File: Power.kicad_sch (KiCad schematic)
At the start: 45 parts, among them J6 Screw_Terminal_01x03, T1 230/6, T2 78250MC-R, U3 LF50_TO252, U4 LD3985G33R_TSOT23, U5 SN6507DGQ, U6 LD3985G33R_TSOT23

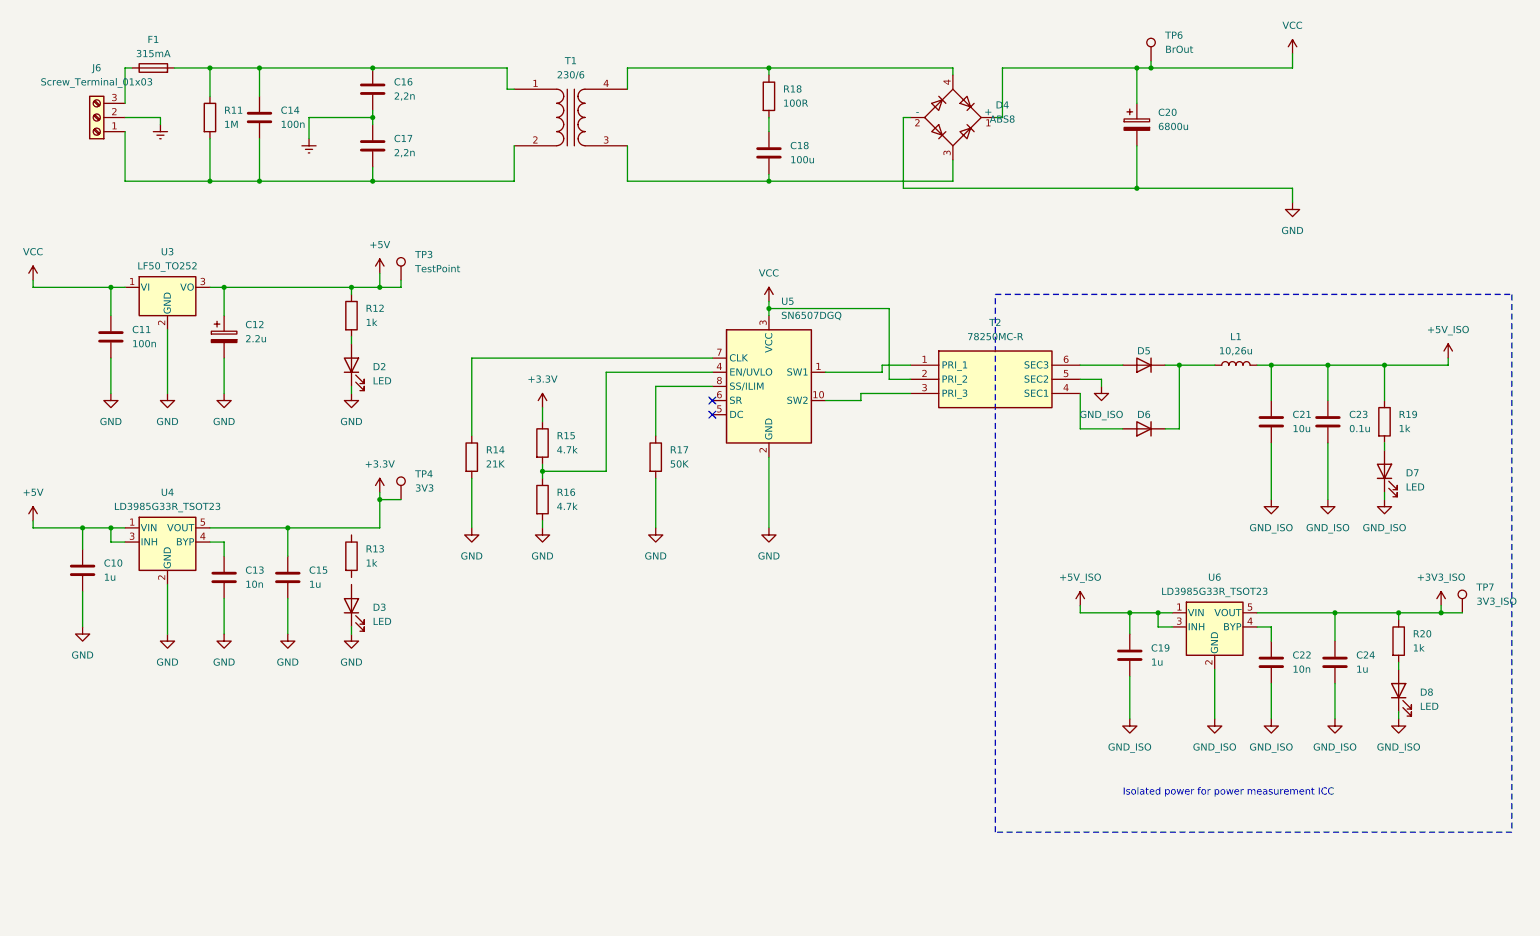
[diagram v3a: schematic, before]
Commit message: Footprints and elements update
Added another batch of footprints and links to the elements. More coming soon.
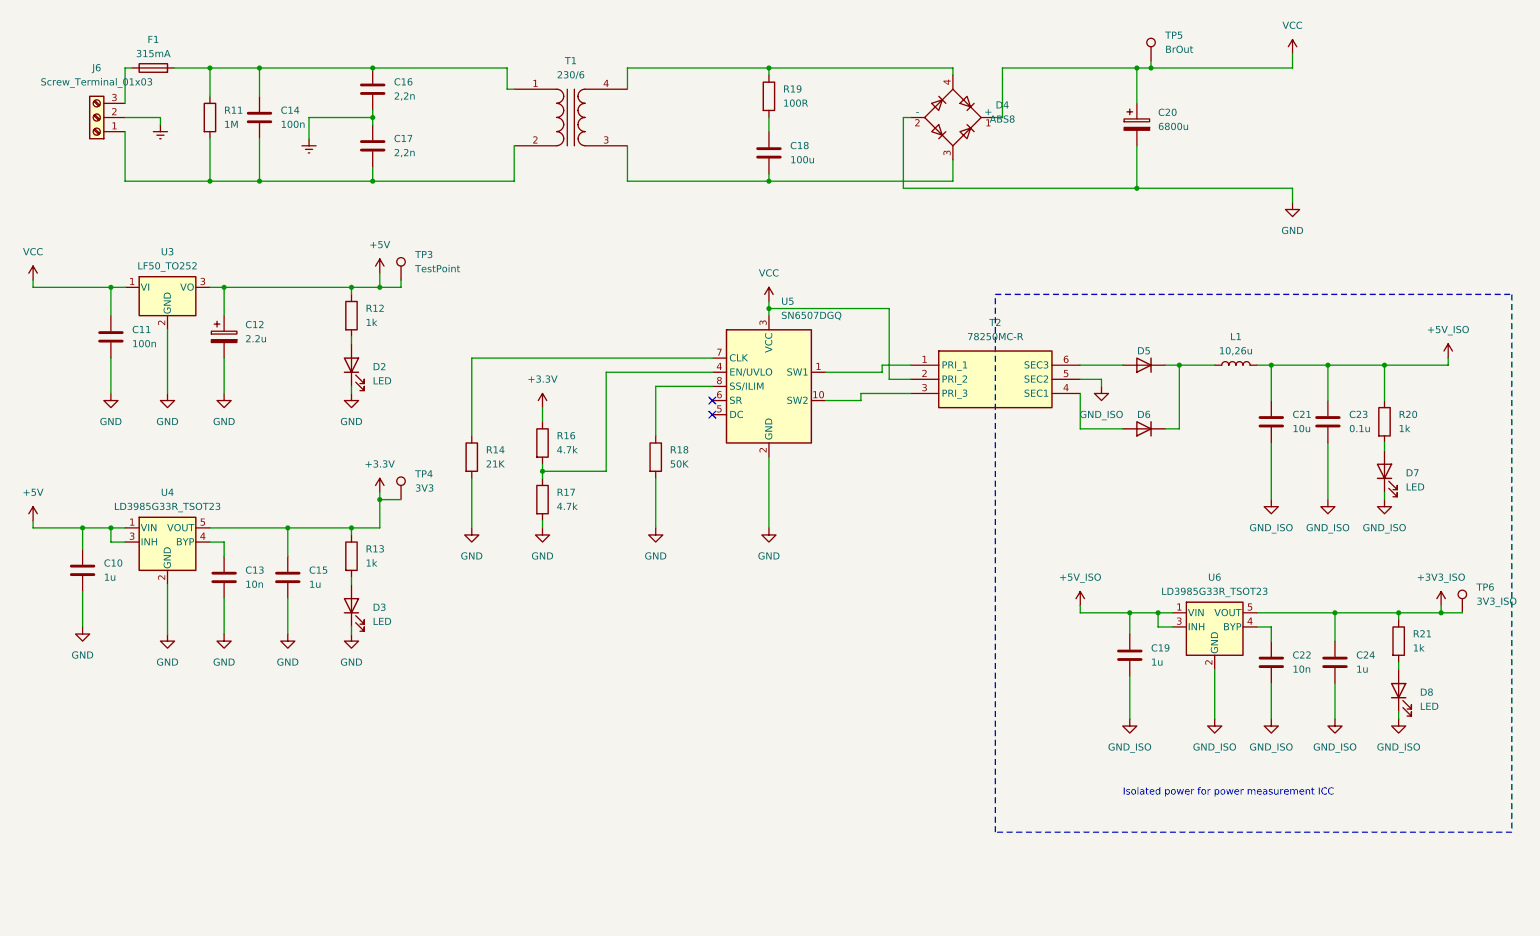
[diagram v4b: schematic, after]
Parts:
- C11, C23: footprint Capacitor_SMD:C_0201_0603Metric_Pad0.64x0.40mm_HandSolder -> Capacitor_SMD:C_0603_1608Metric_Pad1.08x0.95mm_HandSolder
- C18: footprint (none) -> Capacitor_SMD:C_0603_1608Metric_Pad1.08x0.95mm_HandSolder
- R12, R13, R14: footprint (none) -> Resistor_SMD:R_0603_1608Metric_Pad0.98x0.95mm_HandSolder
- R16: renamed from R15; footprint (none) -> Resistor_SMD:R_0603_1608Metric_Pad0.98x0.95mm_HandSolder
- R17: renamed from R16; footprint (none) -> Resistor_SMD:R_0603_1608Metric_Pad0.98x0.95mm_HandSolder
- R18: renamed from R17; footprint (none) -> Resistor_SMD:R_0603_1608Metric_Pad0.98x0.95mm_HandSolder
- R19: renamed from R18; footprint (none) -> Resistor_SMD:R_2512_6332Metric_Pad1.40x3.35mm_HandSolder
- R20: renamed from R19; footprint (none) -> Resistor_SMD:R_0603_1608Metric_Pad0.98x0.95mm_HandSolder
- R21: renamed from R20; footprint (none) -> Resistor_SMD:R_0603_1608Metric_Pad0.98x0.95mm_HandSolder
- renumbered TP6 to TP5, TP7 to TP6
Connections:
- net +3.3V: now also R13.1
- net at R13.2: now also D3.2 (A)
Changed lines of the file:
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@@
   (junction (at 81.28 67.31) (diameter 0) (color 0 0 0 0)
+  )
+  (junction (at 76.2 110.49) (diameter 0) (color 0 0 0 0)
   )
   (junction (at 110.49 100.33) (diameter 0) (color 0 0 0 0)
@@
     (stroke (width 0) (type default))
   )
+  (wire (pts (xy 76.2 110.49) (xy 81.28 110.49))
+    (stroke (width 0) (type default))
+  )
   (wire (pts (xy 241.3 81.28) (xy 251.46 81.28))
     (stroke (width 0) (type default))
@@
     (stroke (width 0) (type default))
   )
-  (wire (pts (xy 64.77 110.49) (xy 81.28 110.49))
+  (wire (pts (xy 64.77 110.49) (xy 76.2 110.49))
     (stroke (width 0) (type default))
   )
@@
     (stroke (width 0) (type default))
   )
+  (wire (pts (xy 76.2 119.38) (xy 76.2 120.65))
+    (stroke (width 0) (type default))
+  )
   (wire (pts (xy 252.73 125.73) (xy 252.73 130.81))
     (stroke (width 0) (type default))
@@
   )
   (wire (pts (xy 167.64 87.63) (xy 167.64 86.36))
+    (stroke (width 0) (type default))
+  )
+  (wire (pts (xy 76.2 110.49) (xy 76.2 111.76))
     (stroke (width 0) (type default))
   )
@@
   (symbol (lib_id "Connector:TestPoint") (at 219.71 26.67 0) (unit 1)
     (in_bom yes) (on_board yes) (dnp no) (fields_autoplaced)
-    (property "Reference" "TP6" (at 222.25 22.098 0)
+    (property "Reference" "TP5" (at 222.25 22.098 0)
       (effects (font (size 1.27 1.27)) (justify left))
     )
@@
       (project "Eng_Thesis"
         (path "/97bd1b5a-123d-47f8-a974-72569e0e2197/403da9b1-219c-43a2-869b-4f14604ce1cf"
-          (reference "TP6") (unit 1)
+          (reference "TP5") (unit 1)
         )
       )
@@
       (effects (font (size 1.27 1.27)) (justify left))
     )
-    (property "Footprint" "" (at 96.012 97.79 90)
+    (property "Footprint" "Resistor_SMD:R_0603_1608Metric_Pad0.98x0.95mm_HandSolder" (at 96.012 97.79 90)
       (effects (font (size 1.27 1.27)) hide)
     )
@@
       (effects (font (size 1.27 1.27)) (justify left))
     )
-    (property "Footprint" "" (at 74.422 72.39 90)
+    (property "Footprint" "Resistor_SMD:R_0603_1608Metric_Pad0.98x0.95mm_HandSolder" (at 74.422 72.39 90)
       (effects (font (size 1.27 1.27)) hide)
     )
@@
       (effects (font (size 1.27 1.27)) (justify left))
     )
-    (property "Footprint" "Capacitor_SMD:C_0201_0603Metric_Pad0.64x0.40mm_HandSolder" (at 252.4252 95.25 0)
+    (property "Footprint" "Capacitor_SMD:C_0603_1608Metric_Pad1.08x0.95mm_HandSolder" (at 252.4252 95.25 0)
       (effects (font (size 1.27 1.27)) hide)
     )
@@
   (symbol (lib_id "Device:R") (at 110.49 95.25 0) (unit 1)
     (in_bom yes) (on_board yes) (dnp no) (fields_autoplaced)
-    (property "Reference" "R15" (at 113.03 93.98 0)
+    (property "Reference" "R16" (at 113.03 93.98 0)
       (effects (font (size 1.27 1.27)) (justify left))
     )
@@
       (effects (font (size 1.27 1.27)) (justify left))
     )
-    (property "Footprint" "" (at 108.712 95.25 90)
+    (property "Footprint" "Resistor_SMD:R_0603_1608Metric_Pad0.98x0.95mm_HandSolder" (at 108.712 95.25 90)
       (effects (font (size 1.27 1.27)) hide)
     )
@@
       (project "Eng_Thesis"
         (path "/97bd1b5a-123d-47f8-a974-72569e0e2197/403da9b1-219c-43a2-869b-4f14604ce1cf"
-          (reference "R15") (unit 1)
+          (reference "R16") (unit 1)
         )
       )
@@
       (effects (font (size 1.27 1.27)) (justify left))
     )
-    (property "Footprint" "" (at 74.422 115.57 90)
+    (property "Footprint" "Resistor_SMD:R_0603_1608Metric_Pad0.98x0.95mm_HandSolder" (at 74.422 115.57 90)
       (effects (font (size 1.27 1.27)) hide)
     )
@@
   (symbol (lib_id "Device:R") (at 110.49 105.41 0) (unit 1)
     (in_bom yes) (on_board yes) (dnp no) (fields_autoplaced)
-    (property "Reference" "R16" (at 113.03 104.14 0)
+    (property "Reference" "R17" (at 113.03 104.14 0)
       (effects (font (size 1.27 1.27)) (justify left))
     )
@@
       (effects (font (size 1.27 1.27)) (justify left))
     )
-    (property "Footprint" "" (at 108.712 105.41 90)
+    (property "Footprint" "Resistor_SMD:R_0603_1608Metric_Pad0.98x0.95mm_HandSolder" (at 108.712 105.41 90)
       (effects (font (size 1.27 1.27)) hide)
     )
@@
       (project "Eng_Thesis"
         (path "/97bd1b5a-123d-47f8-a974-72569e0e2197/403da9b1-219c-43a2-869b-4f14604ce1cf"
-          (reference "R16") (unit 1)
+          (reference "R17") (unit 1)
         )
       )
@@
   (symbol (lib_id "Device:R") (at 261.62 91.44 0) (unit 1)
     (in_bom yes) (on_board yes) (dnp no) (fields_autoplaced)
-    (property "Reference" "R19" (at 264.16 90.17 0)
+    (property "Reference" "R20" (at 264.16 90.17 0)
       (effects (font (size 1.27 1.27)) (justify left))
     )
@@
       (effects (font (size 1.27 1.27)) (justify left))
     )
-    (property "Footprint" "" (at 259.842 91.44 90)
+    (property "Footprint" "Resistor_SMD:R_0603_1608Metric_Pad0.98x0.95mm_HandSolder" (at 259.842 91.44 90)
       (effects (font (size 1.27 1.27)) hide)
     )
@@
       (project "Eng_Thesis"
         (path "/97bd1b5a-123d-47f8-a974-72569e0e2197/403da9b1-219c-43a2-869b-4f14604ce1cf"
-          (reference "R19") (unit 1)
+          (reference "R20") (unit 1)
         )
       )
@@
   (symbol (lib_id "Device:R") (at 264.16 130.81 0) (unit 1)
     (in_bom yes) (on_board yes) (dnp no) (fields_autoplaced)
-    (property "Reference" "R20" (at 266.7 129.54 0)
+    (property "Reference" "R21" (at 266.7 129.54 0)
       (effects (font (size 1.27 1.27)) (justify left))
     )
@@
       (effects (font (size 1.27 1.27)) (justify left))
     )
-    (property "Footprint" "" (at 262.382 130.81 90)
+    (property "Footprint" "Resistor_SMD:R_0603_1608Metric_Pad0.98x0.95mm_HandSolder" (at 262.382 130.81 90)
       (effects (font (size 1.27 1.27)) hide)
     )
@@
       (project "Eng_Thesis"
         (path "/97bd1b5a-123d-47f8-a974-72569e0e2197/403da9b1-219c-43a2-869b-4f14604ce1cf"
-          (reference "R20") (unit 1)
+          (reference "R21") (unit 1)
         )
       )
@@
       (effects (font (size 1.27 1.27)) (justify left))
     )
-    (property "Footprint" "" (at 152.0952 46.99 0)
+    (property "Footprint" "Capacitor_SMD:C_0603_1608Metric_Pad1.08x0.95mm_HandSolder" (at 152.0952 46.99 0)
       (effects (font (size 1.27 1.27)) hide)
     )
@@
   (symbol (lib_id "Connector:TestPoint") (at 275.59 125.73 0) (unit 1)
     (in_bom yes) (on_board yes) (dnp no) (fields_autoplaced)
-    (property "Reference" "TP7" (at 278.13 121.158 0)
+    (property "Reference" "TP6" (at 278.13 121.158 0)
       (effects (font (size 1.27 1.27)) (justify left))
     )
@@
       (project "Eng_Thesis"
         (path "/97bd1b5a-123d-47f8-a974-72569e0e2197/403da9b1-219c-43a2-869b-4f14604ce1cf"
-          (reference "TP7") (unit 1)
+          (reference "TP6") (unit 1)
         )
       )
@@
   (symbol (lib_id "Device:R") (at 130.81 97.79 0) (unit 1)
     (in_bom yes) (on_board yes) (dnp no) (fields_autoplaced)
-    (property "Reference" "R17" (at 133.35 96.52 0)
+    (property "Reference" "R18" (at 133.35 96.52 0)
       (effects (font (size 1.27 1.27)) (justify left))
     )
@@
       (effects (font (size 1.27 1.27)) (justify left))
     )
-    (property "Footprint" "" (at 129.032 97.79 90)
+    (property "Footprint" "Resistor_SMD:R_0603_1608Metric_Pad0.98x0.95mm_HandSolder" (at 129.032 97.79 90)
       (effects (font (size 1.27 1.27)) hide)
     )
@@
       (project "Eng_Thesis"
         (path "/97bd1b5a-123d-47f8-a974-72569e0e2197/403da9b1-219c-43a2-869b-4f14604ce1cf"
-          (reference "R17") (unit 1)
+          (reference "R18") (unit 1)
         )
       )
@@
   (symbol (lib_id "Device:R") (at 151.13 33.02 0) (unit 1)
     (in_bom yes) (on_board yes) (dnp no) (fields_autoplaced)
-    (property "Reference" "R18" (at 153.67 31.75 0)
+    (property "Reference" "R19" (at 153.67 31.75 0)
       (effects (font (size 1.27 1.27)) (justify left))
     )
@@
       (effects (font (size 1.27 1.27)) (justify left))
     )
-    (property "Footprint" "" (at 149.352 33.02 90)
-      (effects (font (size 1.27 1.27)) hide)
-    )
-    (property "Datasheet" "~" (at 151.13 33.02 0)
-      (effects (font (size 1.27 1.27)) hide)
-    )
-    (pin "1")
-    (pin "2")
-    (instances
-      (project "Eng_Thesis"
-        (path "/97bd1b5a-123d-47f8-a974-72569e0e2197/403da9b1-219c-43a2-869b-4f14604ce1cf"
-          (reference "R18") (unit 1)
+    (property "Footprint" "Resistor_SMD:R_2512_6332Metric_Pad1.40x3.35mm_HandSolder" (at 149.352 33.02 90)
+      (effects (font (size 1.27 1.27)) hide)
+    )
+    (property "Datasheet" "https://www.tme.eu/pl/details/sp12-100r-5%25/rezystory-smd/royal-ohm/sp123wj0101t1e/" (at 151.13 33.02 0)
+      (effects (font (size 1.27 1.27)) hide)
+    )
+    (pin "1")
+    (pin "2")
+    (instances
+      (project "Eng_Thesis"
+        (path "/97bd1b5a-123d-47f8-a974-72569e0e2197/403da9b1-219c-43a2-869b-4f14604ce1cf"
+          (reference "R19") (unit 1)
         )
       )
@@
       (effects (font (size 1.27 1.27)) (justify left))
     )
-    (property "Footprint" "Capacitor_SMD:C_0201_0603Metric_Pad0.64x0.40mm_HandSolder" (at 33.9852 80.01 0)
-      (effects (font (size 1.27 1.27)) hide)
-    )
+    (property "Footprint" "Capacitor_SMD:C_0603_1608Metric_Pad1.08x0.95mm_HandSolder" (at 33.9852 80.01 0)
+      (effects (font (size 1.27 1.27)) hide)
+    )

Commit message: 1st complete version of schematic with footprints
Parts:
- J6: footprint (none) -> LibLoader:XY126V-3P
- R11: footprint (none) -> Resistor_SMD:R_1206_3216Metric_Pad1.30x1.75mm_HandSolder
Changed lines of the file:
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@@
       (effects (font (size 1.27 1.27)) (justify left))
     )
-    (property "Footprint" "" (at 49.022 36.83 90)
-      (effects (font (size 1.27 1.27)) hide)
-    )
-    (property "Datasheet" "~" (at 50.8 36.83 0)
+    (property "Footprint" "Resistor_SMD:R_1206_3216Metric_Pad1.30x1.75mm_HandSolder" (at 49.022 36.83 90)
+      (effects (font (size 1.27 1.27)) hide)
+    )
+    (property "Datasheet" "https://www.tme.eu/pl/details/rv1206fr-071ml/rezystory-smd/yageo/" (at 50.8 36.83 0)
       (effects (font (size 1.27 1.27)) hide)
     )
@@
       (effects (font (size 1.27 1.27)))
     )
-    (property "Footprint" "" (at 30.48 36.83 0)
-      (effects (font (size 1.27 1.27)) hide)
-    )
-    (property "Datasheet" "~" (at 30.48 36.83 0)
-      (effects (font (size 1.27 1.27)) hide)
-    )
+    (property "Footprint" "LibLoader:XY126V-3P" (at 30.48 36.83 0)
+      (effects (font (size 1.27 1.27)) hide)
+    )
+    (property "Datasheet" "https://www.tme.eu/pl/details/xy126v-3p-5.0-gn/listwy-zaciskowe-do-druku/xinya/xy126v-3p-5-0mm-green/" (at 30.48 36.83 0)
+      (effects (font (size 1.27 1.27)) hide)
+    )
